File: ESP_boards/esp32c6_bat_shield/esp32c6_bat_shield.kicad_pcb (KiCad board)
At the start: 2 copper layers, 45 x 38 mm, 3 parts, among them J1 USB_C_Receptacle_USB2.0_16P

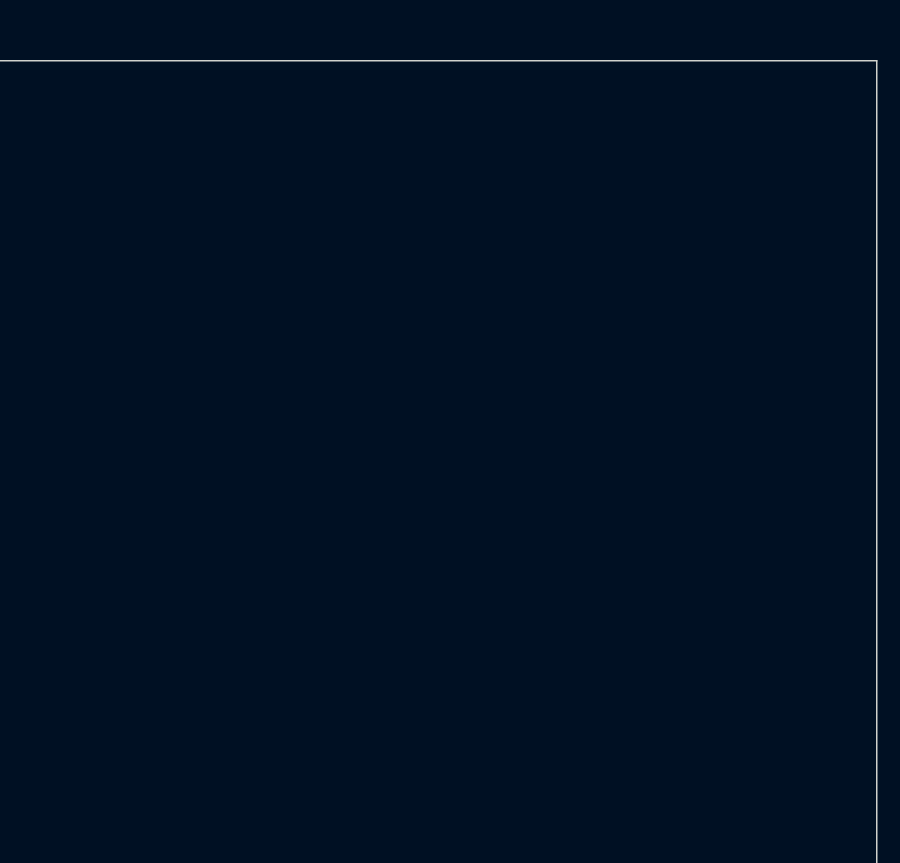
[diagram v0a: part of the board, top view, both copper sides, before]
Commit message: Added esp32c6-mini to library
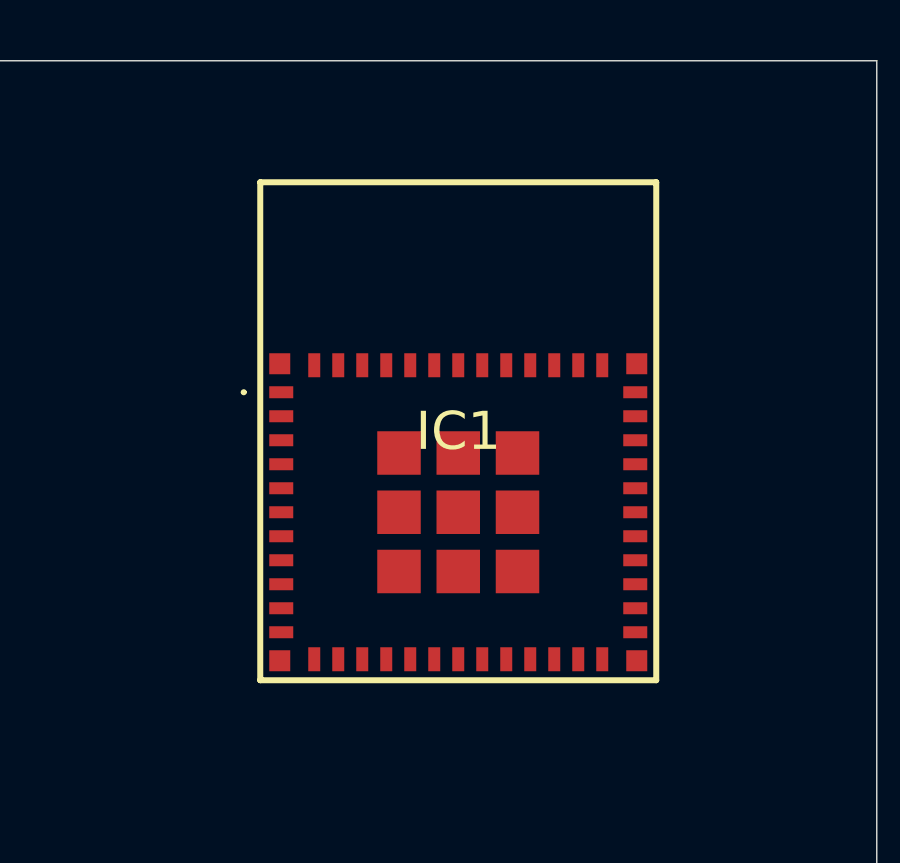
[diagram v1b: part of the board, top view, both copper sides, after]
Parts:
- added IC1: ESP32-C6-MINI-1-H4, MCU_espressif_moma:ESP32C6MINI1H4, F.Cu at (131.1, 62.4)
